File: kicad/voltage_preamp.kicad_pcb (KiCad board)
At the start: 2 copper layers, 31 parts, among them J1 Conn_Coaxial, J2 Conn_01x01_Male, J3 Conn_01x01_Male, J4 Conn_01x01_Male, J5 Conn_Coaxial, J6 Conn_01x02_Male, U1 lmp7721, U2 lmp7721, U3 lmp7721, U4 lt1028, U5 MAX6033

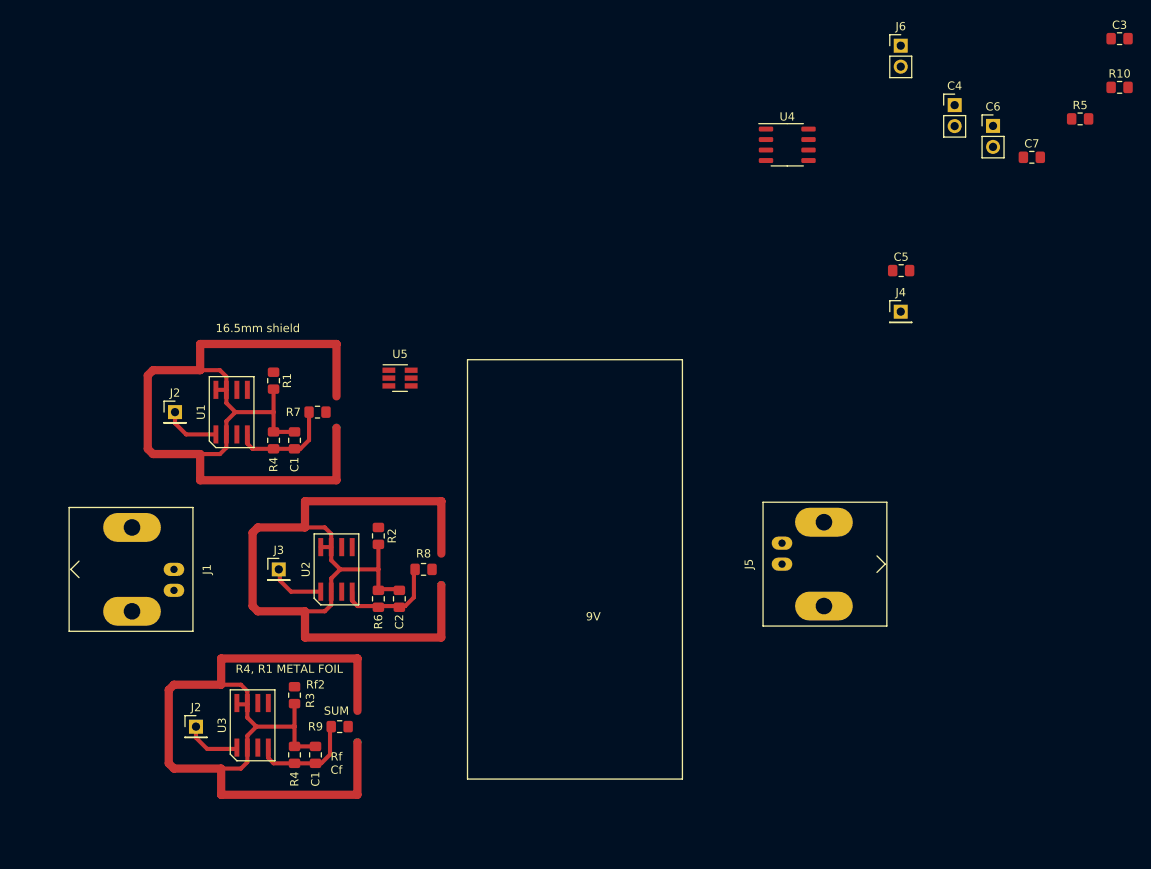
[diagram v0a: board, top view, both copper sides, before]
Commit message: v1 schematic and layout complete, simulated
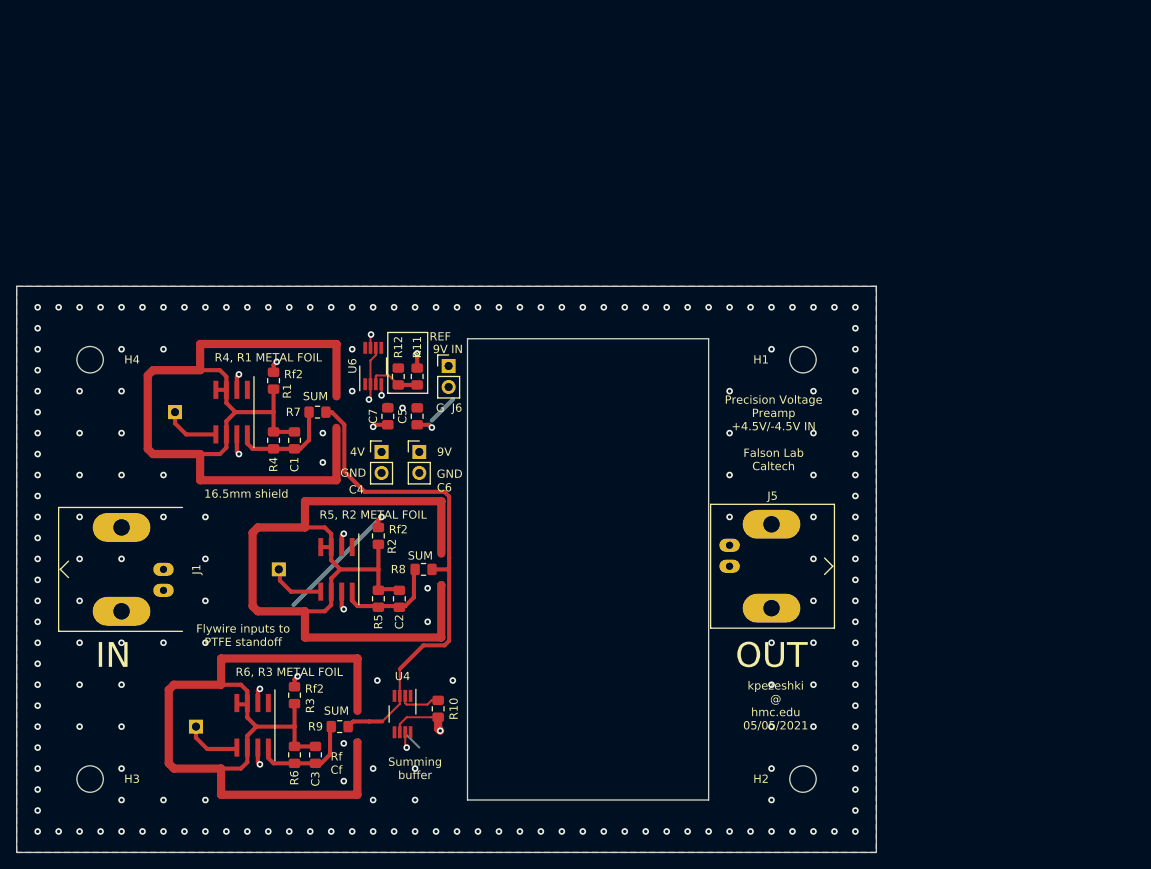
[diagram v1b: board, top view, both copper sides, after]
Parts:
- removed the C1 at (145.4, 166.0)
- removed the J2 at (130.9, 162.6)
- removed the R4 at (142.9, 166.0)
- removed U5: MAX6033, Package_TO_SOT_SMD:SOT-23-6_Handsoldering
- added H1: MountingHole, MountingHole:MountingHole_3.2mm_M3, F.Cu at (204.5, 118.1)
- added H2: MountingHole, MountingHole:MountingHole_3.2mm_M3_DIN965, F.Cu at (204.5, 168.9)
- added H3: MountingHole, MountingHole:MountingHole_3.2mm_M3, F.Cu at (118.1, 168.9)
- added H4: MountingHole, MountingHole:MountingHole_3.2mm_M3, F.Cu at (118.1, 118.1)
- added R11: 15k, Resistor_SMD:R_0805_2012Metric_Pad1.15x1.40mm_HandSolder, F.Cu at (157.7, 120.1)
- added R12: 15k, Resistor_SMD:R_0805_2012Metric_Pad1.15x1.40mm_HandSolder, F.Cu at (155.4, 120.1)
- added U6: OPA211, Package_SO:VSSOP-8_3.0x3.0mm_P0.65mm, F.Cu at (152.4, 118.9)
- U4: value lt1028 -> OPA211; footprint Package_SO:SO-8_3.9x4.9mm_P1.27mm -> Package_SO:VSSOP-8_3.0x3.0mm_P0.65mm
- moved C3 130.4 mm to (145.4, 166.0), turned to 270 degrees
- moved R10 111.7 mm to (160.3, 160.4), turned to 90 degrees
- moved R5 103.0 mm to (153.0, 147.1), turned to 270 degrees
- moved J4 99.1 mm to (130.9, 162.6)
- moved C7 84.1 mm to (154.2, 125.0), turned to 90 degrees
- moved U4 83.2 mm to (156.0, 161.0), turned to 270 degrees
- moved C4 81.2 mm to (153.4, 129.3)
- moved C6 79.9 mm to (158.0, 129.3)
- moved J6 67.1 mm to (161.5, 118.9)
- moved C5 61.2 mm to (157.7, 125.0), turned to 90 degrees
- moved R6 21.5 mm to (142.9, 166.0)
- moved J5 6.36 mm to (195.6, 143.1)
- moved J1 1.27 mm to (127.0, 143.5)
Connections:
- U1 pad 5: Net-(U1-Pad5) -> (no net)
- U4 pad 8: (no net) -> GND
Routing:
- net Net-(C1-Pad1): track 312.9 -> 104.3 mm
- net Net-(C3-Pad1): track 0.00 -> 104.3 mm
- net Net-(C2-Pad1): track 0.00 -> 104.3 mm
- net +4V: track 0.00 -> 103.2 mm, vias 0 -> 5
- net Net-(J5-Pad1): track 0.00 -> 77.8 mm, vias 0 -> 1
- net Net-(R7-Pad1): track 0.00 -> 61.1 mm
- net Net-(C1-Pad2): track 40.1 -> 13.4 mm
- net GND: track 0.00 -> 14.4 mm, vias 0 -> 195
- net Net-(C2-Pad2): track 0.00 -> 13.4 mm
- net Net-(C3-Pad2): track 0.00 -> 13.4 mm
- net +9V: track 0.00 -> 13.2 mm, vias 0 -> 7
- net Net-(J2-Pad1): track 13.7 -> 6.86 mm
- net Net-(J4-Pad1): track 0.00 -> 6.86 mm
- net Net-(R11-Pad2): track 0.00 -> 6.49 mm
- net Net-(R10-Pad2): track 0.00 -> 5.16 mm
- added copper zone on In1.Cu, net +4V
- added copper zone on In2.Cu, net +9V
- added copper zone on B.Cu, net GND
- added copper zone on F.Cu, net GND
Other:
- board outline added: 104.1 x 68.6 mm
- copper layers 2 -> 4
- board text added: "4V"
- board text added: "Flywire inputs to PTFE standoff"
- board text added: "G"
- board text added: "GND"
- board text added: "IN"
- board text added: "OUT"
- board text added: "Precision Voltage Preamp +4.5V/-4.5V IN Falson Lab Caltech"
- board text added: "R5, R2 METAL FOIL"
- board text added: "R6, R3 METAL FOIL"
- board text added: "REF"
- board text added: "Summing buffer"
- board text added: "kpezeshki @ hmc.edu 05/05/2021"

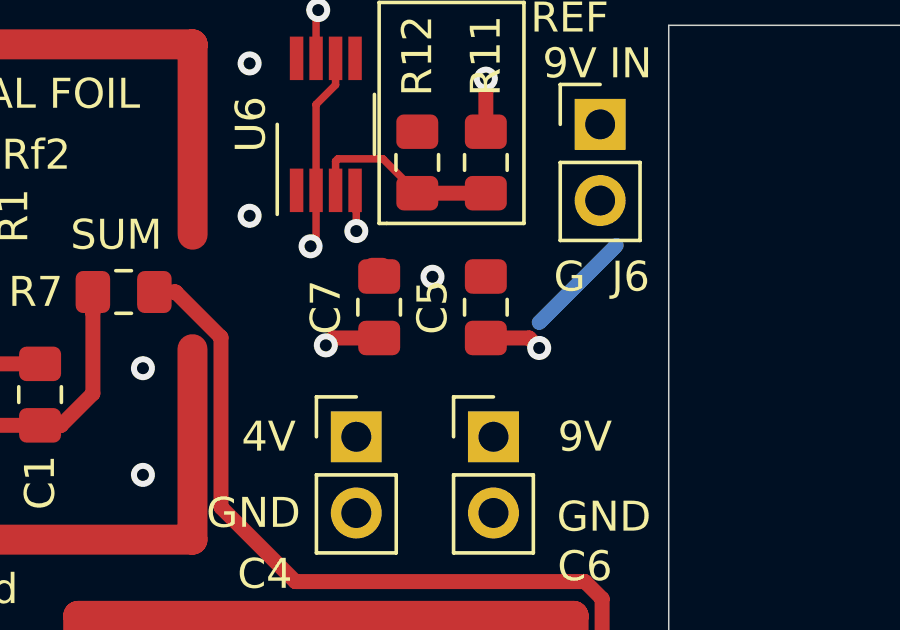
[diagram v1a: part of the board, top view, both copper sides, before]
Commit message: fixed bypass cap network
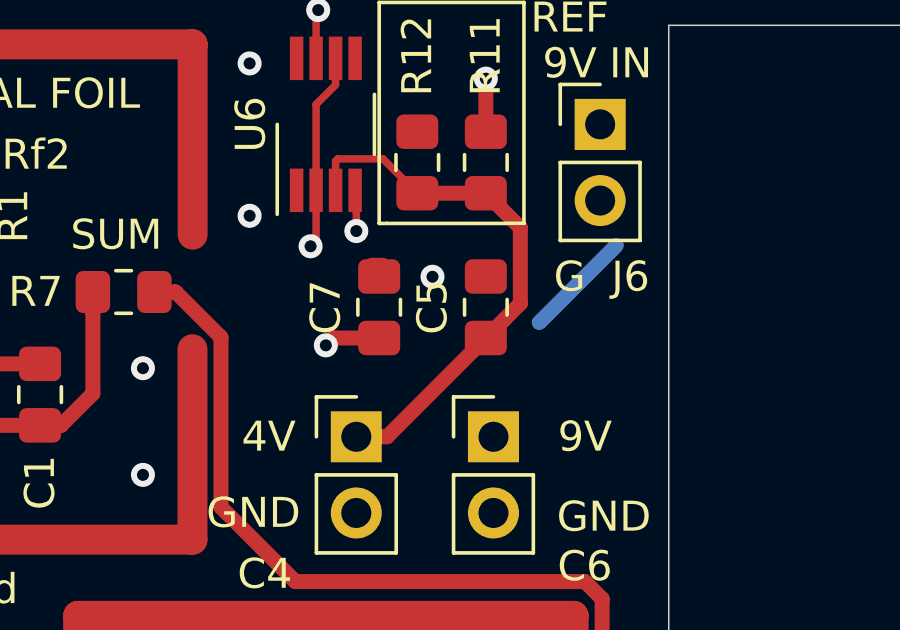
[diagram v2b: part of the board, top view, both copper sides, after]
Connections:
- C4 pad 1: +4V -> /4VRES
- C5 pad 1: +4V -> /4VRES
- R11 pad 2: Net-(R11-Pad2) -> /4VRES
- R12 pad 1: Net-(R11-Pad2) -> /4VRES
- U6 pad 3: Net-(R11-Pad2) -> /4VRES
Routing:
- net /4VRES: track 0.00 -> 18.0 mm
- net Net-(R11-Pad2): track 6.49 -> 0.00 mm
- net +4V: track 103.2 -> 101.3 mm, vias 5 -> 4
